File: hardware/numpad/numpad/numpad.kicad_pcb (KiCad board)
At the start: 2 copper layers, 119.1 x 138.1 mm, 81 parts, among them SW1 ROT_SKYLOONG_HS, Y1 8MHz

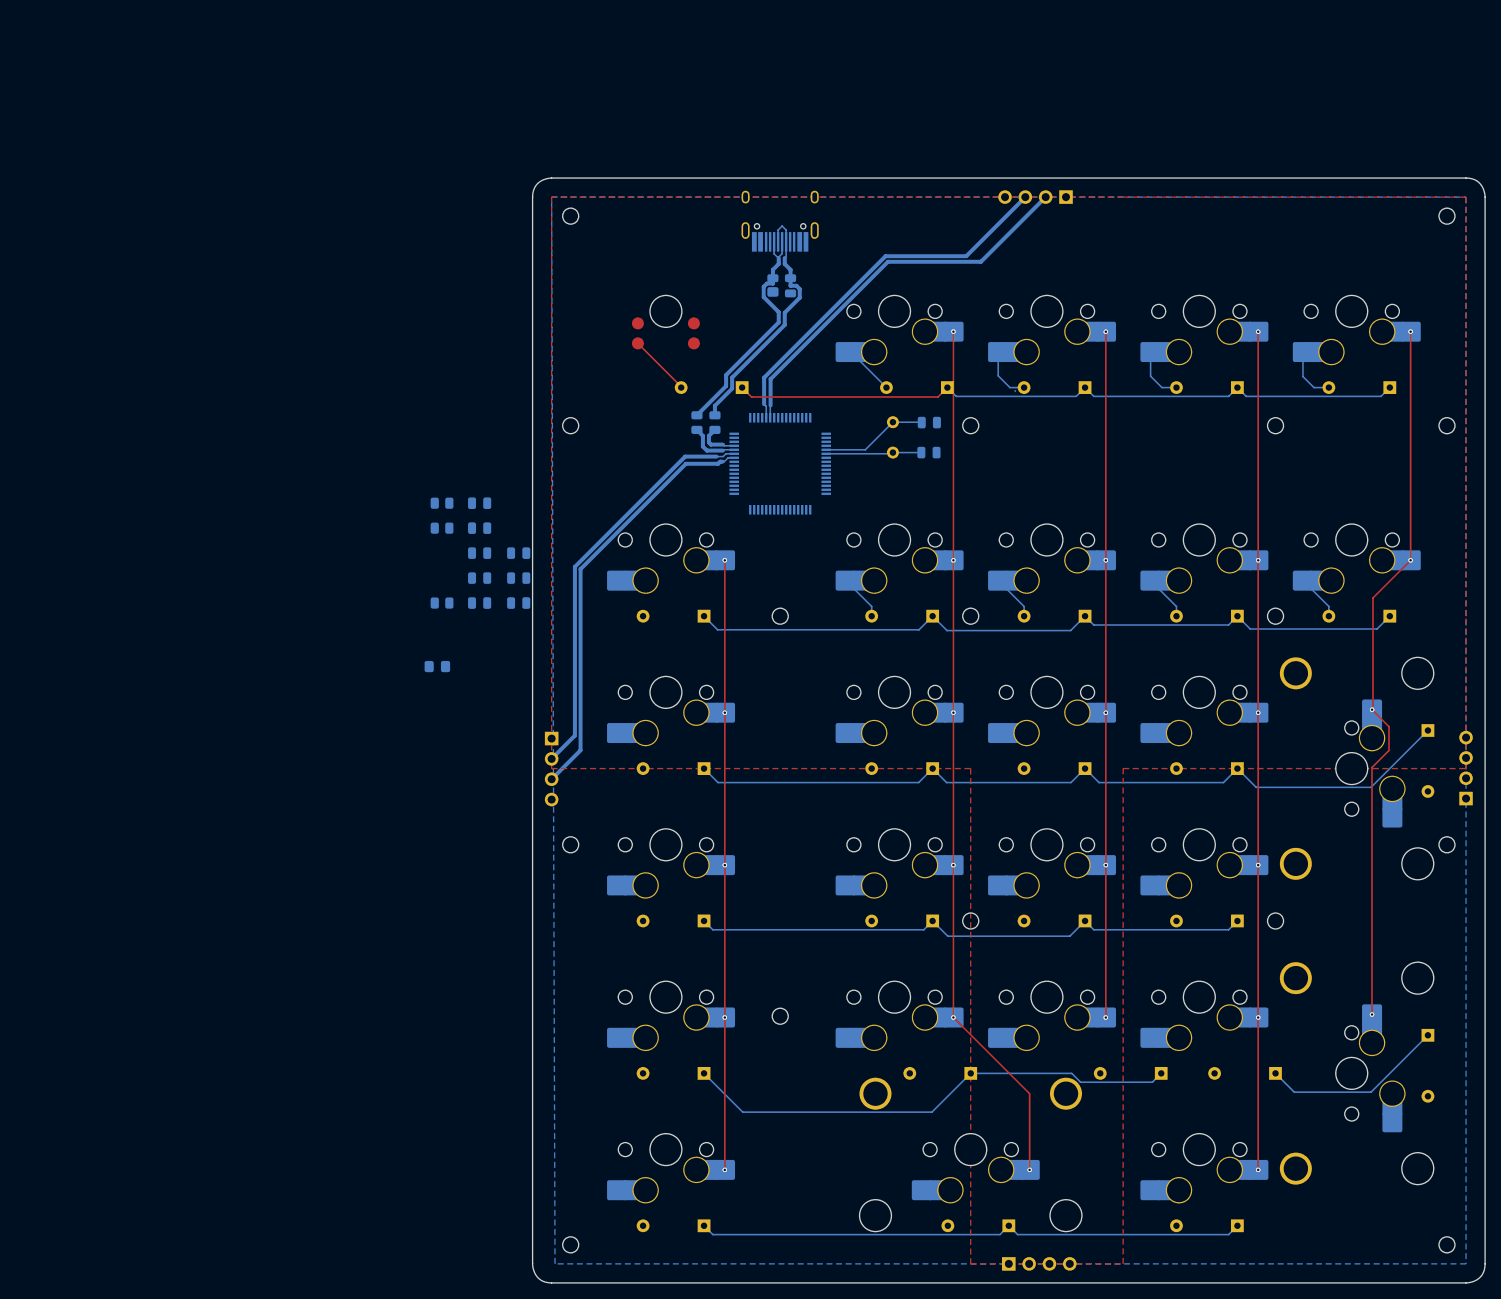
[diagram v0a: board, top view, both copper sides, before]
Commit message: rgb matrix and drc rules
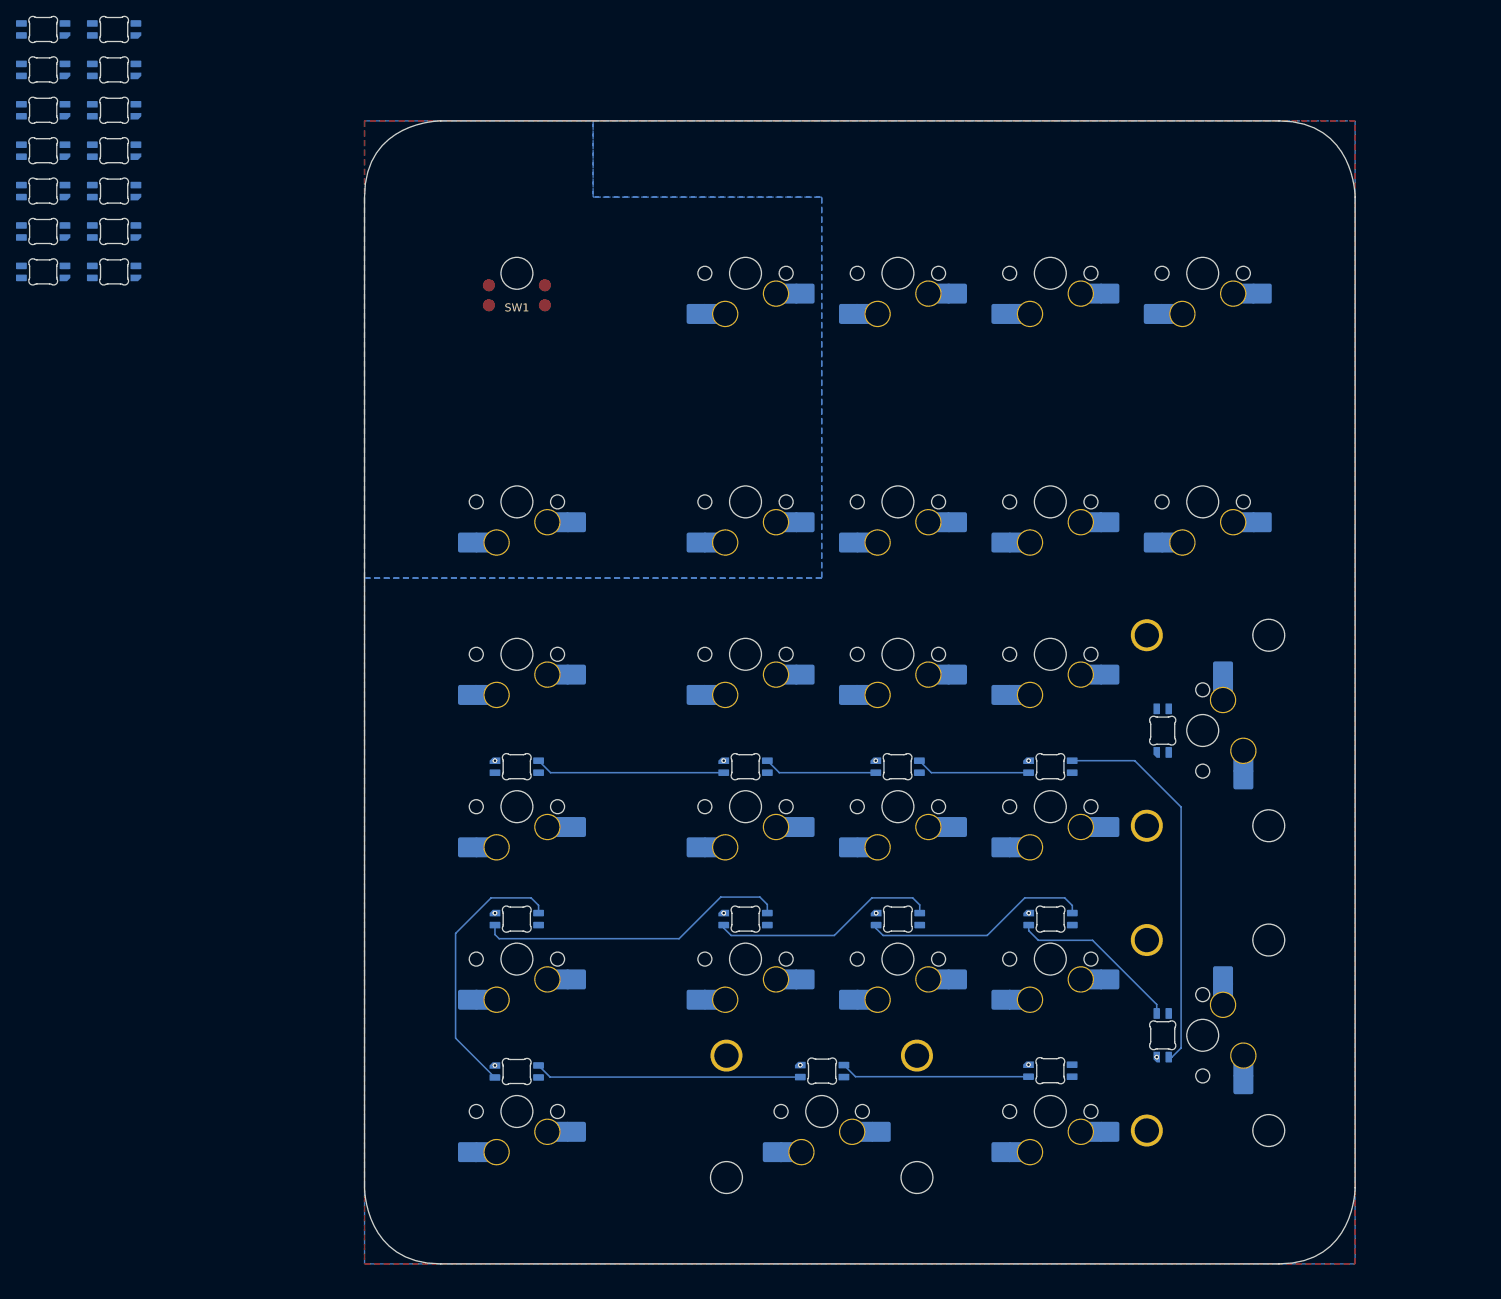
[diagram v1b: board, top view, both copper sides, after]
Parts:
- removed C1, C2: 20pF, PCM_Capacitor_SMD_AKL:C_0805_2012Metric
- removed C10, C7: 1uF, PCM_Capacitor_SMD_AKL:C_0805_2012Metric
- removed C3, C4, C5, C6: 100nF, PCM_Capacitor_SMD_AKL:C_0805_2012Metric
- removed C8: 10uF, PCM_Capacitor_SMD_AKL:C_0805_2012Metric
- removed C9: 4.7uF, PCM_Capacitor_SMD_AKL:C_0805_2012Metric
- removed D1: PRTR5V0U2X, PCM_Package_TO_SOT_SMD_AKL:SOT-143
- removed D10, D11, D12, D13, D14, D15, D16, D17, D18, D19, D20, D21, D22, D23, D24, D25, D26, D27, D28, D29, D3, D4, D5, D6, D7, D8, D9: 1N4148, PCM_Diode_THT_AKL:D_DO-35_SOD27_P7.62mm_Horizontal
- removed East1, North1, South1, West1: Conn_01x04, Connector_PinSocket_2.54mm:PinSocket_1x04_P2.54mm_Vertical
- removed FB1: Ferrite_Bead, PCM_Fuse_AKL:Fuse_0805_2012Metric_Pad1.15x1.40mm_BigPads
- removed R1, R2: 5.1k, PCM_Resistor_SMD_AKL:R_0805_2012Metric
- removed R3, R4: 22, PCM_Resistor_SMD_AKL:R_0805_2012Metric
- removed R5: 10k, PCM_Resistor_SMD_AKL:R_0805_2012Metric
- removed U1: ~, footprints:LQFP64-10x10mm
- removed USB1: HRO-TYPE-C-31-M-12, Type-C.pretty-master:HRO-TYPE-C-31-M-12-HandSoldering
- removed Y1: 8MHz, PCM_Crystal_AKL:Crystal_HC52-U_Vertical
- added LED1: MX_SK6812MINI-E, PCM_marbastlib-mx:LED_MX_6028R, B.Cu at (-2.73, 17.1)
- added LED10: MX_SK6812MINI-E, PCM_marbastlib-mx:LED_MX_6028R, B.Cu at (-11.6, 27.2)
- added LED11: MX_SK6812MINI-E, PCM_marbastlib-mx:LED_MX_6028R, B.Cu at (-11.6, 32.3)
- added LED12: MX_SK6812MINI-E, PCM_marbastlib-mx:LED_MX_6028R, B.Cu at (-11.6, 37.4)
- added LED13: MX_SK6812MINI-E, PCM_marbastlib-mx:LED_MX_6028R, B.Cu at (-11.6, 42.4)
- added LED14: MX_SK6812MINI-E, PCM_marbastlib-mx:LED_MX_6028R, B.Cu at (-11.6, 47.5)
- added LED15: MX_SK6812MINI-E, PCM_marbastlib-mx:LED_MX_6028R, B.Cu at (128.3, 104.8)
- added LED16: MX_SK6812MINI-E, PCM_marbastlib-mx:LED_MX_6028R, B.Cu at (114.3, 109.3)
- added LED17: MX_SK6812MINI-E, PCM_marbastlib-mx:LED_MX_6028R, B.Cu at (95.2, 109.3)
- added LED18: MX_SK6812MINI-E, PCM_marbastlib-mx:LED_MX_6028R, B.Cu at (76.2, 109.3)
- added LED19: MX_SK6812MINI-E, PCM_marbastlib-mx:LED_MX_6028R, B.Cu at (47.6, 109.3)
- added LED2: MX_SK6812MINI-E, PCM_marbastlib-mx:LED_MX_6028R, B.Cu at (-2.73, 22.2)
- added LED20: MX_SK6812MINI-E, PCM_marbastlib-mx:LED_MX_6028R, B.Cu at (85.8, 147.3)
- added LED21: MX_SK6812MINI-E, PCM_marbastlib-mx:LED_MX_6028R, B.Cu at (128.3, 142.9)
- added LED22: MX_SK6812MINI-E, PCM_marbastlib-mx:LED_MX_6028R, B.Cu at (114.3, 128.3)
- added LED23: MX_SK6812MINI-E, PCM_marbastlib-mx:LED_MX_6028R, B.Cu at (95.2, 128.3)
- added LED24: MX_SK6812MINI-E, PCM_marbastlib-mx:LED_MX_6028R, B.Cu at (76.2, 128.3)
- added LED25: MX_SK6812MINI-E, PCM_marbastlib-mx:LED_MX_6028R, B.Cu at (47.6, 128.3)
- added LED26: MX_SK6812MINI-E, PCM_marbastlib-mx:LED_MX_6028R, B.Cu at (114.3, 147.3)
- added LED27: MX_SK6812MINI-E, PCM_marbastlib-mx:LED_MX_6028R, B.Cu at (47.6, 147.4)
- added LED3: MX_SK6812MINI-E, PCM_marbastlib-mx:LED_MX_6028R, B.Cu at (-2.73, 27.2)
- added LED4: MX_SK6812MINI-E, PCM_marbastlib-mx:LED_MX_6028R, B.Cu at (-2.73, 32.3)
- added LED5: MX_SK6812MINI-E, PCM_marbastlib-mx:LED_MX_6028R, B.Cu at (-2.73, 37.4)
- added LED6: MX_SK6812MINI-E, PCM_marbastlib-mx:LED_MX_6028R, B.Cu at (-2.73, 42.4)
- added LED7: MX_SK6812MINI-E, PCM_marbastlib-mx:LED_MX_6028R, B.Cu at (-2.73, 47.5)
- added LED8: MX_SK6812MINI-E, PCM_marbastlib-mx:LED_MX_6028R, B.Cu at (-11.6, 17.1)
- added LED9: MX_SK6812MINI-E, PCM_marbastlib-mx:LED_MX_6028R, B.Cu at (-11.6, 22.2)
- moved S3 66.4 mm to (85.7, 152.4), turned to 0 degrees
- moved S2 32.3 mm to (133.3, 142.9), turned to 90 degrees
- moved NUM_3 19.2 mm to (114.3, 133.3)
- moved MACRO_C1 19.2 mm to (114.3, 47.6)
- moved NUM_10 19.2 mm to (114.3, 95.2)
- moved NUM_6 19.2 mm to (114.3, 114.3)
- moved NUM_MULT1 19.2 mm to (114.3, 76.2)
- moved NUM_0 19.2 mm to (85.7, 152.4)
- moved NUM_PERIOD1 19.2 mm to (114.3, 152.4)
- moved MACRO_H1 19.2 mm to (47.6, 133.3)
- moved NUM_1 19.2 mm to (76.2, 133.3)
- moved NUM_2 19.2 mm to (95.2, 133.3)
- moved MACRO_A1 19.2 mm to (76.2, 47.6)
- moved MACRO_B1 19.2 mm to (95.2, 47.6)
- moved MACRO_D1 19.2 mm to (133.3, 47.6)
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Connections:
- net /Numpad Matrix + Rotary Encoder/COL1 renamed /COL1
- net /Numpad Matrix + Rotary Encoder/COL2 renamed /COL2
- net /Numpad Matrix + Rotary Encoder/COL3 renamed /COL3
- net /Numpad Matrix + Rotary Encoder/COL4 renamed /COL4
- net /Numpad Matrix + Rotary Encoder/COL5 renamed /COL5
- net /Numpad Matrix + Rotary Encoder/ROT+ renamed /ROT_TIMA
- net /Numpad Matrix + Rotary Encoder/ROT- renamed /ROT_TIMB
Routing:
- net /COL2: track 108.7 -> 0.00 mm, vias 6 -> 0
- net /COL4: track 104.8 -> 0.00 mm, vias 6 -> 0
- net /Numpad Matrix + Rotary Encoder/ROW3: track 98.8 -> 0.00 mm
- net /Numpad Matrix + Rotary Encoder/ROW2: track 90.9 -> 0.00 mm
- net /COL5: track 89.1 -> 0.00 mm, vias 4 -> 0
- net /COL3: track 85.7 -> 0.00 mm, vias 5 -> 0
- net /Numpad Matrix + Rotary Encoder/ROW5: track 85.0 -> 0.00 mm
- net /Numpad Matrix + Rotary Encoder/ROW1: track 84.7 -> 0.00 mm
- net /COL1: track 76.2 -> 0.00 mm, vias 5 -> 0
- net /Numpad Matrix + Rotary Encoder/ROW4: track 70.1 -> 0.00 mm
- net /Numpad Matrix + Rotary Encoder/ROW6: track 68.5 -> 0.00 mm
- net /UART_TX_EAST: track 52.7 -> 0.00 mm
- net /UART_RX_EAST: track 51.0 -> 0.00 mm
- net /UART_RX_NORTH: track 48.7 -> 0.00 mm
- net Net-(LED16-DOUT): track 0.00 -> 48.2 mm
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- added copper zone on B.Cu, net +3.3V
- added copper zone on B.Cu, net +5V
- added copper zone on F.Cu, net GND
- removed copper zone on F.Cu, net +5V
- removed copper zone on B.Cu, net GND
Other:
- board size 119.1 x 138.1 mm -> 123.8 x 142.9 mm
- copper layers 2 -> 4
